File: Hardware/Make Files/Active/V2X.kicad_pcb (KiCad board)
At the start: 2 copper layers, 85 x 56 mm, 216 parts, among them CON1 AVR-PDI-6, IC1 ATXMEGA16A4U-A, J1 DB9, P10 Board Mount 2, P11 Ficudial2, P12 Board Mount 3, P13 Ficudial3, P14 5V0_OUT, P15 Board Mount 4, P16 Ficudial4, P17 CUR_SEN, P19 CUR_SEN, P20 Jumper 1, P21 Jumper 2, P22 CONN_02X04, P23 Jumper 3, P24 Jumper 4, P25 CONN_02X08, P5 NVM_RST, P6 Board Mount 1, P7 Ficudial1, P9 USB_u, Q1 2N7000, Q10 2N3904, Q11 IRF9335, Q13 BSS84, Q14 IRF9335, Q15 2N7000, Q16 2N7000, Q17 2N7000, Q18 2N7000, Q19 2N7000, Q2 BSS84, Q3 BSS84, Q4 BSS84, Q5 3906, Q6 2N3904, Q7 2N7000, Q8 2N3904, Q9 2N3904, SW1 SPST, SW2 SW_PUSH, U1 FT4232H, U10 MCP2551, U11 XRP6124, U12 SLG59M, U15 SLG59M, U16 SLG59M, U17 XRP6124, U18 SLG59M, U19 ADXL345, U2 93C46, U20 USB2242, U21 74LS126, U22 74HC595, U23 74HC595, U5 ESDAxxSC6, U6 ESDAxxSC6, U7 STN1110, U8 LM339, U9 LM317, X1 12MHz, X2 16MHz, X3 24MHz

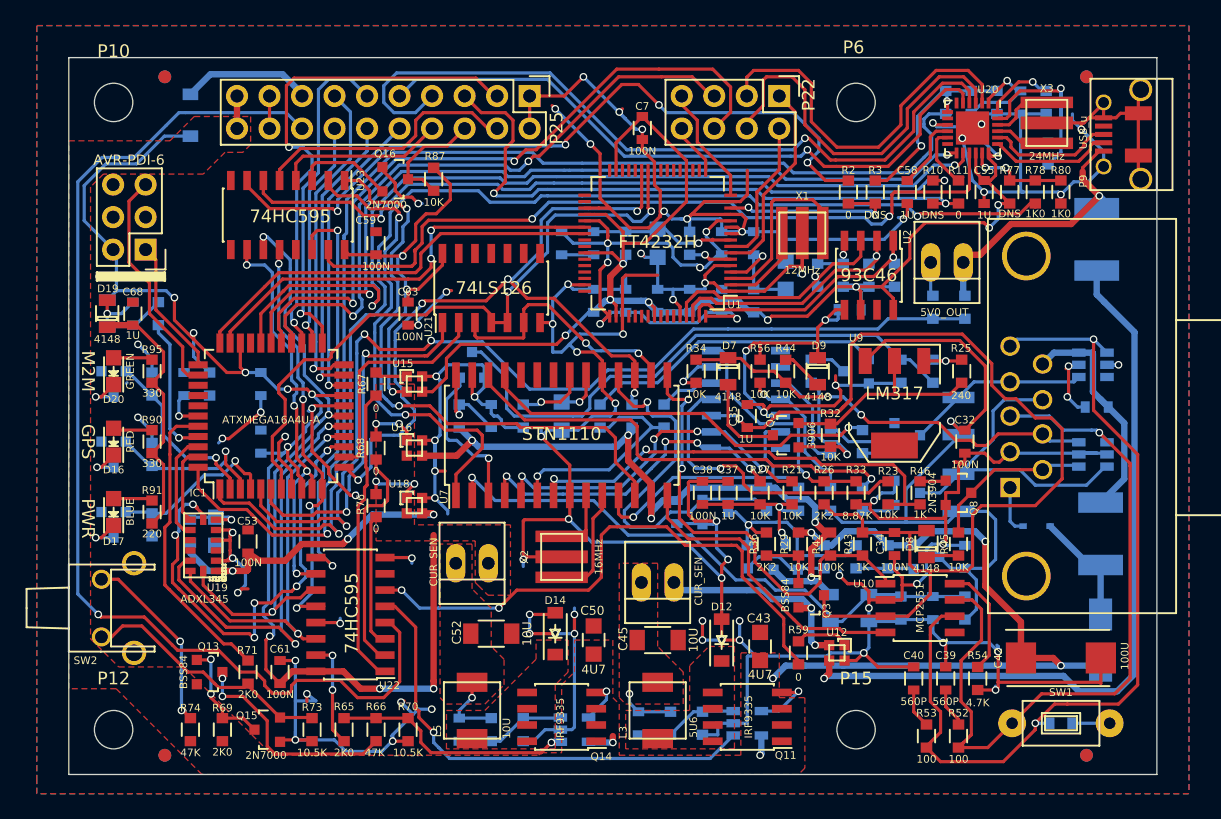
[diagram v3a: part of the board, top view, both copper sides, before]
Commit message: Added USB-A to design
discovered the Rpi cannot be back fed over USB, had to add a power Port
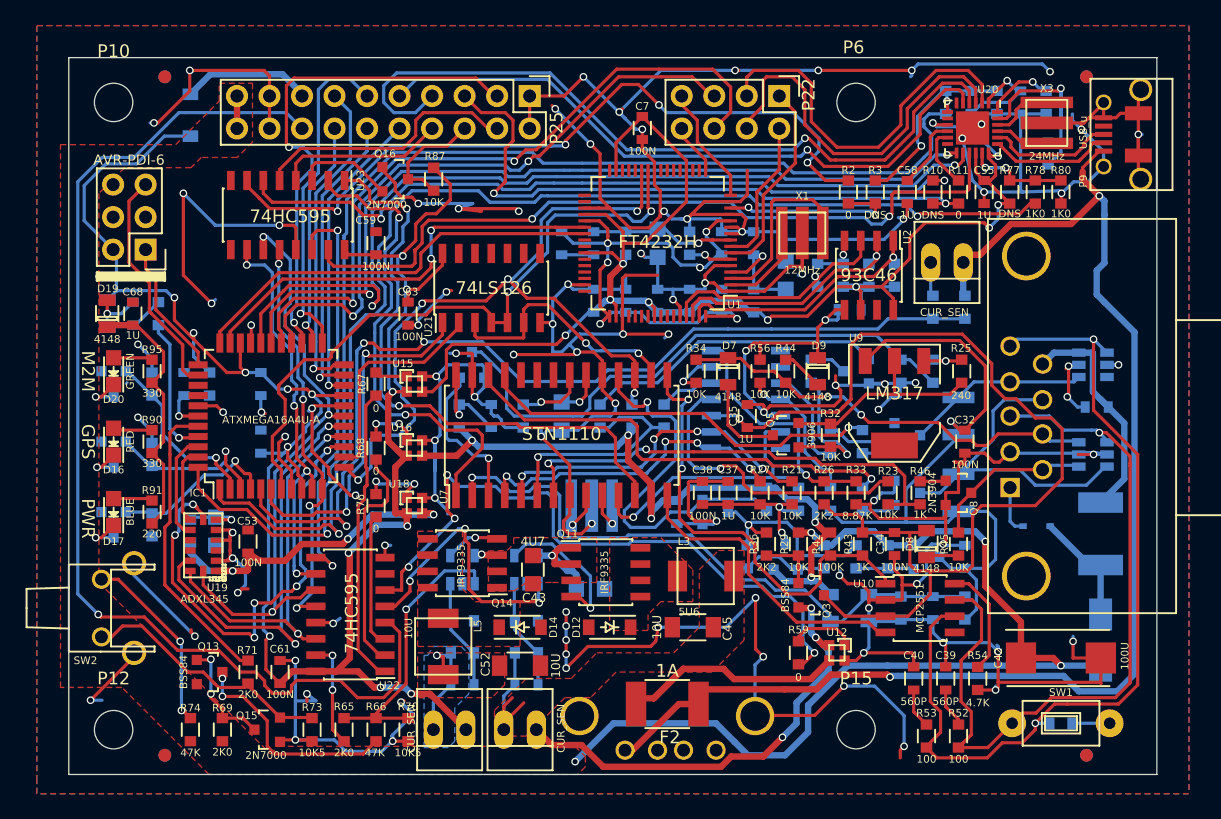
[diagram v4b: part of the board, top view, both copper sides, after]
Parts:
- added P8: USB_A, Connect:USB_A, B.Cu at (78.7, 177.1)
- C50, X2: moved to B.Cu
- F1: value 1.1A -> 1.25A
- F2: moved to F.Cu
- P14: value 5V0_OUT -> CUR_SEN
- R62, R70, R73: value 10.5K -> 10K5
- moved F2 49.4 mm to (82.0, 173.5), turned to 0 degrees
- moved U11 21.0 mm to (71.0, 163.0), turned to 90 degrees
- moved C43 18.7 mm to (71.5, 163.0), turned to 270 degrees
- moved R61 15.9 mm to (71.0, 167.0), turned to 180 degrees
- moved Q11 15.8 mm to (77.2, 163.2), turned to 0 degrees
- moved P17 15.7 mm to (70.5, 175.5)
- moved U17 15.3 mm to (66.0, 163.0), turned to 90 degrees
- moved Q14 14.3 mm to (66.0, 162.5)
- moved P19 13.1 mm to (65.0, 175.5)
- moved R62 12.5 mm to (71.0, 169.5), turned to 180 degrees
- moved L3 11.1 mm to (85.0, 163.5), turned to 0 degrees
- moved R75 9.74 mm to (66.0, 167.0), turned to 0 degrees
- moved C44 9.25 mm to (71.0, 172.0), turned to 0 degrees
- moved D12 8.81 mm to (77.5, 167.5), turned to 180 degrees
- moved R72 6.41 mm to (66.0, 169.5), turned to 0 degrees
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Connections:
- net CAN_RXD_PS renamed CAN_RXD_SEQ
- CON1 pad 3: (no net) -> Net-(CON1-Pad3)
- CON1 pad 4: (no net) -> Net-(CON1-Pad4)
- IC1 pad 36: (no net) -> Net-(IC1-Pad36)
- IC1 pad 37: (no net) -> Net-(IC1-Pad37)
- J1 pad : GND -> (no net)
- P10 pad 1: (no net) -> Net-(P10-Pad1)
- P12 pad 1: (no net) -> Net-(P12-Pad1)
- P14 pad 1: 5V0_B_OUT -> 4V1_B
- P14 pad 2: GND -> Net-(C46-Pad1)
- P15 pad 1: (no net) -> Net-(P15-Pad1)
- P6 pad 1: (no net) -> Net-(P6-Pad1)
- P9 pad 4: (no net) -> Net-(P9-Pad4)
- U1 pad 18: (no net) -> Net-(U1-Pad18)
- U1 pad 19: (no net) -> Net-(U1-Pad19)
- U1 pad 21: (no net) -> Net-(U1-Pad21)
- U1 pad 22: (no net) -> Net-(U1-Pad22)
- U1 pad 23: (no net) -> Net-(U1-Pad23)
- U1 pad 24: (no net) -> Net-(U1-Pad24)
- U1 pad 28: (no net) -> Net-(U1-Pad28)
- U1 pad 29: (no net) -> Net-(U1-Pad29)
- U1 pad 30: (no net) -> Net-(U1-Pad30)
- U1 pad 32: (no net) -> Net-(U1-Pad32)
- U1 pad 33: (no net) -> Net-(U1-Pad33)
- U1 pad 34: (no net) -> Net-(U1-Pad34)
- U1 pad 40: (no net) -> Net-(U1-Pad40)
- U1 pad 41: (no net) -> Net-(U1-Pad41)
- U1 pad 43: (no net) -> Net-(U1-Pad43)
- U1 pad 44: (no net) -> Net-(U1-Pad44)
- U1 pad 45: (no net) -> Net-(U1-Pad45)
- U1 pad 46: (no net) -> Net-(U1-Pad46)
- U1 pad 48: (no net) -> Net-(U1-Pad48)
- U1 pad 52: (no net) -> Net-(U1-Pad52)
- U1 pad 53: (no net) -> Net-(U1-Pad53)
- U1 pad 54: (no net) -> Net-(U1-Pad54)
- U1 pad 55: (no net) -> Net-(U1-Pad55)
- U1 pad 57: (no net) -> Net-(U1-Pad57)
- U1 pad 58: (no net) -> Net-(U1-Pad58)
- U1 pad 59: (no net) -> Net-(U1-Pad59)
- U10 pad 5: (no net) -> Net-(U10-Pad5)
- U20 pad 12: (no net) -> Net-(U20-Pad12)
- U20 pad 6: (no net) -> Net-(U20-Pad6)
- U20 pad 8: (no net) -> Net-(U20-Pad8)
- U22 pad 7: (no net) -> Net-(U22-Pad7)
- U23 pad 9: (no net) -> Net-(U23-Pad9)
- U6 pad 3: (no net) -> Net-(U6-Pad3)
- U7 pad 22: (no net) -> Net-(U7-Pad22)
- U7 pad 23: (no net) -> Net-(U7-Pad23)
- U7 pad 24: (no net) -> Net-(U7-Pad24)
- U8 pad 14: (no net) -> Net-(U8-Pad14)
- U8 pad 8: (no net) -> Net-(U8-Pad8)
- U8 pad 9: (no net) -> Net-(U8-Pad9)
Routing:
- net GND: track 579.0 -> 668.5 mm, vias 81 -> 99
- net 5V0_B_OUT: track 23.3 -> 99.9 mm, vias 1 -> 2
- net 5V0_B: track 60.0 -> 20.3 mm, vias 1 -> 0
- net 12V0_B: track 63.1 -> 92.1 mm
- net 3V3_A: track 138.8 -> 158.4 mm, vias 12 -> 14
- net 5V0_A: track 16.8 -> 35.9 mm, vias 2 -> 3
- net 5V0_EN: track 37.7 -> 21.7 mm, vias 1 -> 3
- net 5V0_B_EN: track 44.6 -> 52.4 mm, vias 2 -> 4
- net Net-(C44-Pad1): track 4.86 -> 11.9 mm, vias 1 -> 0
- net Net-(Q11-Pad1): track 4.88 -> 11.7 mm
- net CAN_CLKN: track 8.83 -> 3.92 mm, vias 0 -> 1
- net 4V1_B: track 0.00 -> 4.40 mm
- net Net-(C51-Pad1): track 5.71 -> 9.69 mm
- net Net-(C46-Pad1): track 0.00 -> 3.76 mm
- net Net-(R65-Pad2): track 18.9 -> 22.0 mm
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- added copper zone on B.Cu, net Net-(C51-Pad1)
- removed copper zone on F.Cu, net 3V3_A

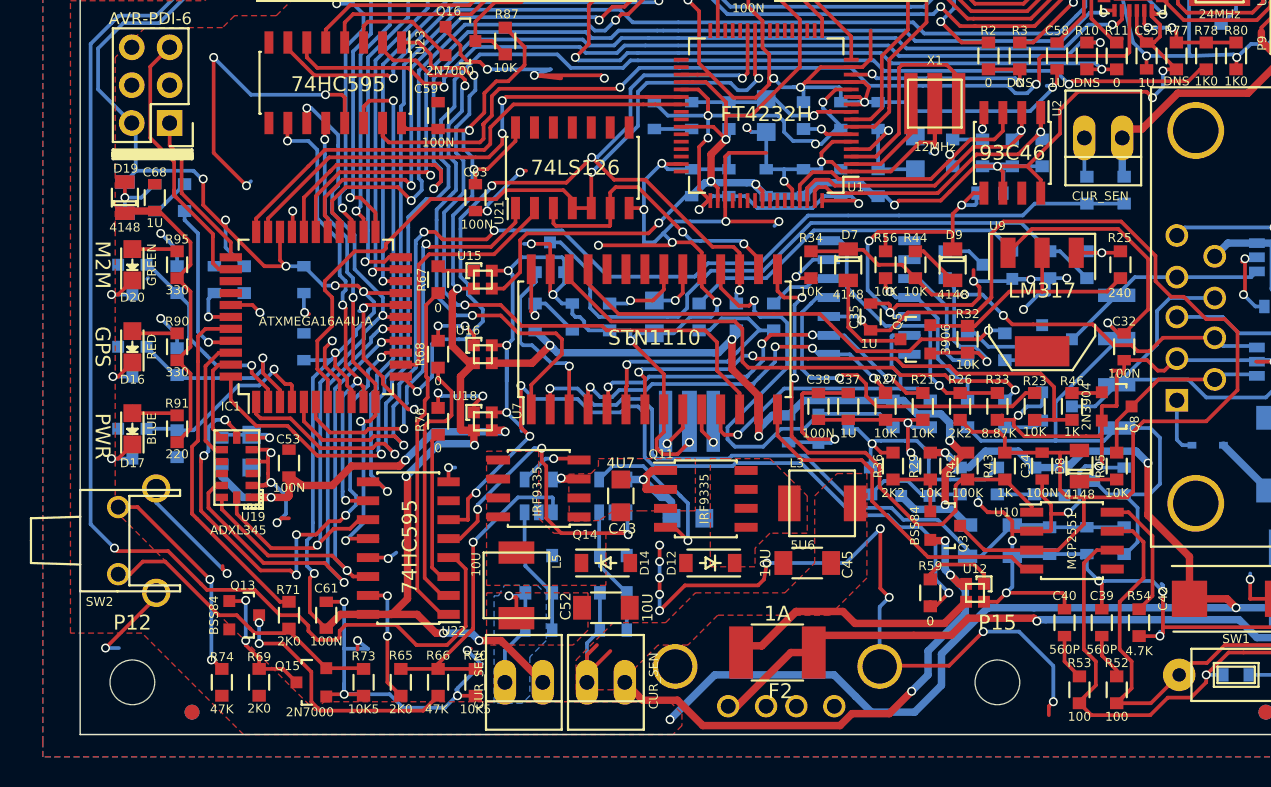
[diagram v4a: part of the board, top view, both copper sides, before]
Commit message: No Rpi Backpower fix
added a USB-A to the board to power the HOST. fixed LED labeling.
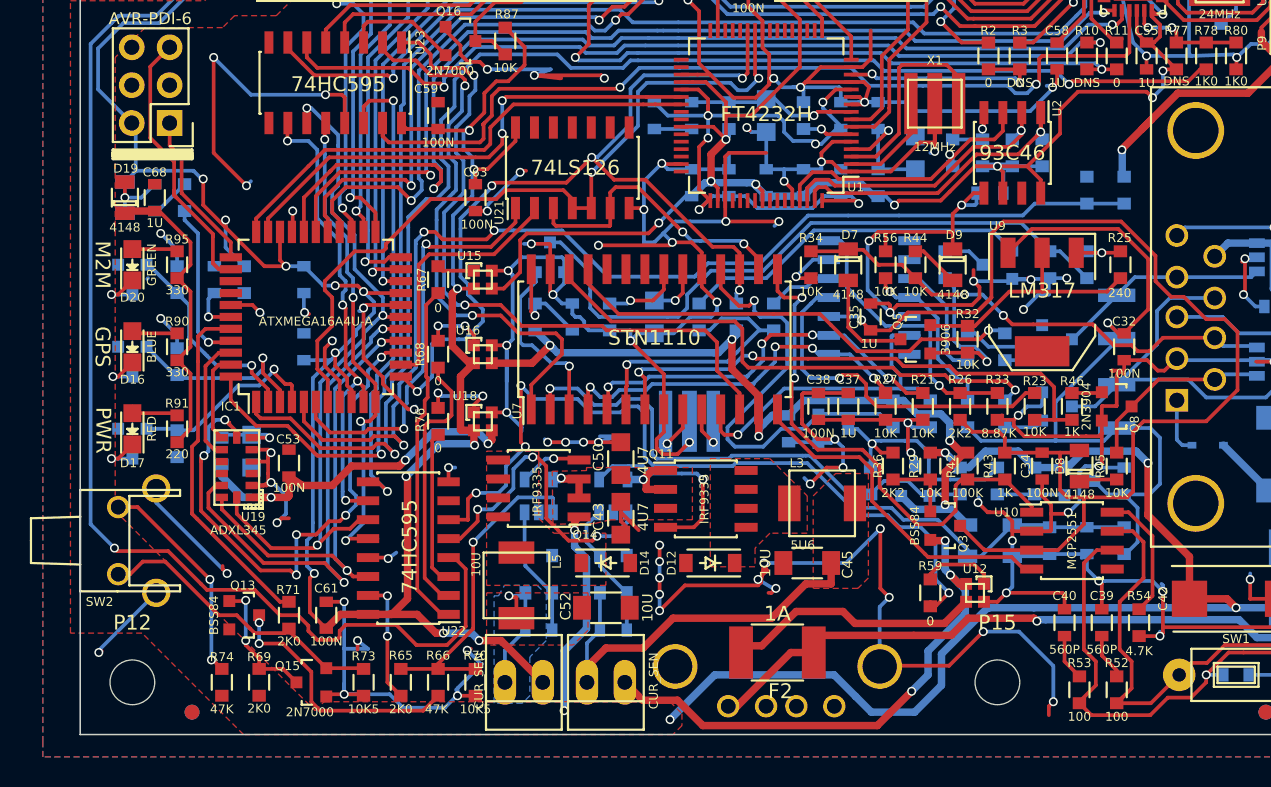
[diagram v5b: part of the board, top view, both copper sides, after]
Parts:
- removed P14: CUR_SEN, Connect:PINHEAD1-2
- C50: moved to F.Cu
- D16: value RED -> BLUE
- D17: value BLUE -> RED
- moved C50 6.02 mm to (71.5, 160.5), turned to 90 degrees
- moved C43 1.50 mm to (71.5, 164.5)
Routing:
- net GND: track 668.5 -> 687.6 mm, vias 99 -> 107
- net Net-(C44-Pad1): track 11.9 -> 28.0 mm
- net 12V0_B: track 92.1 -> 103.5 mm, vias 6 -> 8
- net 5V0_B_OUT: track 99.9 -> 104.5 mm, vias 2 -> 3
- net 4V1_B: track 4.40 -> 0.00 mm
- net Net-(C46-Pad1): track 3.76 -> 0.00 mm
- net 5V0_B: track 20.3 -> 17.1 mm
- net Net-(Q11-Pad1): track 11.7 -> 13.7 mm
- net Net-(C44-Pad2): track 8.67 -> 9.44 mm
- net 3V3_D: track 25.6 -> 24.9 mm
- net 5V0_EN: track 21.7 -> 21.0 mm
- net 5V0_B_EN: track 52.4 -> 53.1 mm
- net CAN_RX: track 23.7 -> 23.1 mm
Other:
- board text added: "JAGUAR LAND ROVER OSTC RVI V2X V1.2 2015"
- board text removed: "JAGUR LAND ROVER OSTC RVI V2X V1.2 2015"

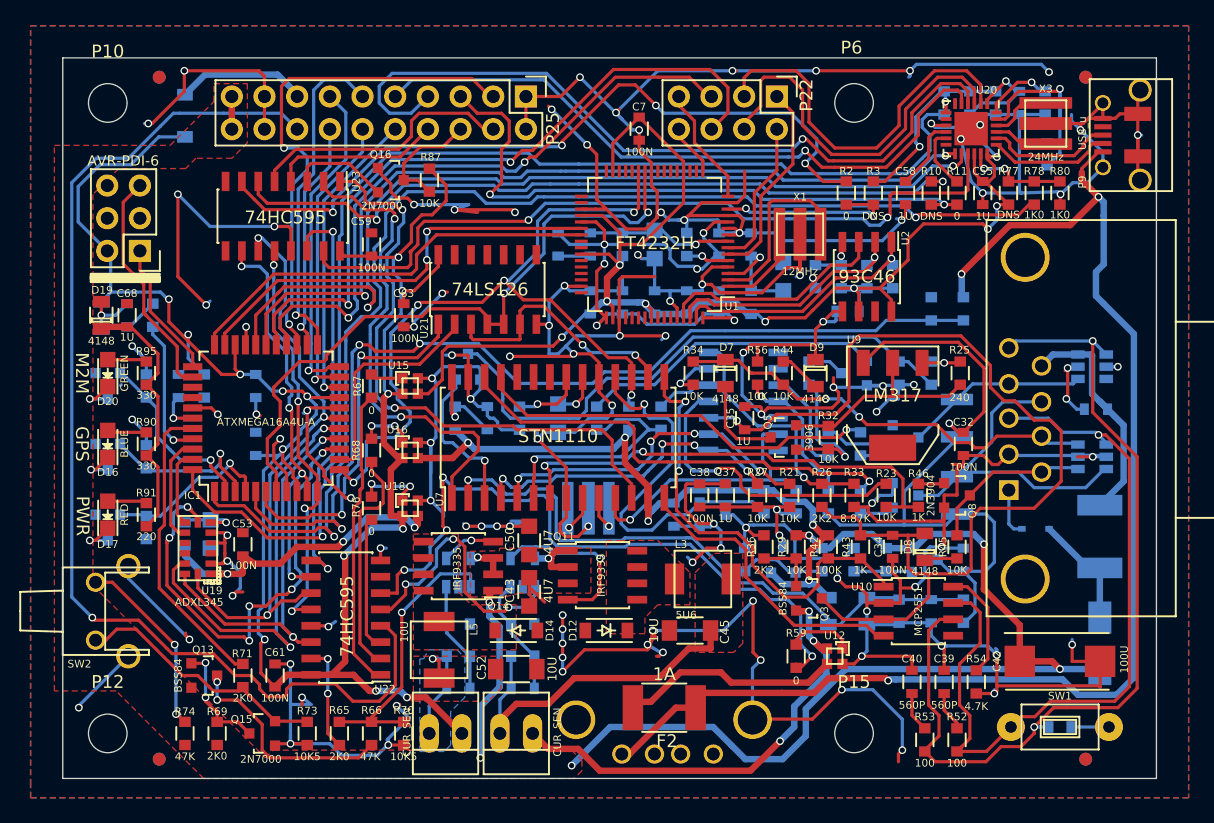
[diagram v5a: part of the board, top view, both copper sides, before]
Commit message: Verification findings and modifications
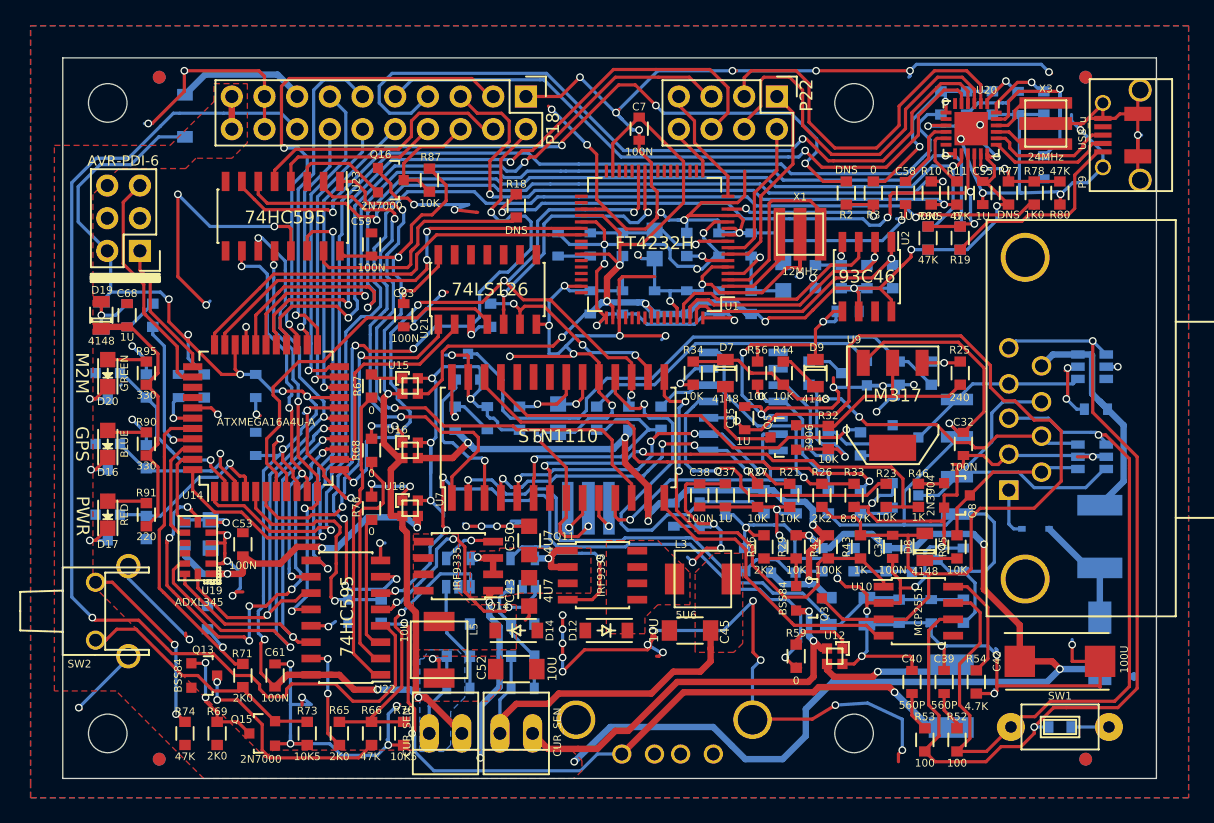
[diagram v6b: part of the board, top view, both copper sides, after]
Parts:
- added C65: 10N, Custom Parts:R_0603_sm, B.Cu at (46.5, 166.5)
- added R18: DNS, Custom Parts:R_0603_sm, F.Cu at (70.5, 134.5)
- added R19: 47K, Custom Parts:R_0603_sm, F.Cu at (105.0, 137.0)
- added R60: 47K, Custom Parts:R_0603_sm, F.Cu at (102.5, 137.0)
- added R63: 1K, Custom Parts:R_0603_sm, B.Cu at (68.5, 143.0)
- added R64: DNS, Custom Parts:R_0603_sm, B.Cu at (102.5, 137.0)
- added R97: DNS, Custom Parts:R_0603_sm, B.Cu at (105.0, 137.0)
- added REF**: Symbol_OSHW-Logo_SilkScreen_BIG, Symbols:Symbol_OSHW-Logo_SilkScreen_BIG, B.Cu at (57.8, 129.8)
- F2: moved to B.Cu
- R2: value 0 -> DNS
- R3: value DNS -> 0
- R80, R83: value 1K0 -> 47K
- moved R88 51.0 mm to (60.0, 166.0), turned to 270 degrees
- moved R89 51.0 mm to (57.5, 166.0), turned to 90 degrees
- moved F2 22.3 mm to (104.3, 172.6), turned to 270 degrees
- moved C56 1.03 mm to (111.5, 131.5), turned to 270 degrees
- moved R81 0.25 mm to (105.5, 126.5)
- moved R82 0.25 mm to (103.5, 126.5)
- moved R83 0.25 mm to (107.5, 126.5)
- moved C57 0.10 mm to (109.5, 126.5)
- moved R79 0.10 mm to (111.5, 126.5)
- turned R2 to 90 degrees
- turned R3 to 270 degrees
- turned R80 to 270 degrees
- renumbered P25 to P18, IC1 to U14
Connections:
- net SEQ-CHGPUMP renamed SEQ_CHGPUMP
- P18 pad 2: GND -> SIM_WAKE
- P9 pad 1: 5V0_B_OUT -> 5V0_HOST
- R2 pad 1: ~FTDI_RESET -> Net-(R2-Pad1)
- R2 pad 2: Net-(R2-Pad2) -> ~FTDI_RESET
- R3 pad 1: Net-(R2-Pad2) -> HUB_PWR_PRT1
- R3 pad 2: HUB_PWR_PRT1 -> Net-(R2-Pad1)
- R80 pad 1: GND -> HUB_SUSP_IND
- R80 pad 2: HUB_SUSP_IND -> GND
- U1 pad 14: Net-(R2-Pad2) -> Net-(R2-Pad1)
- U14 pad 13: CAN_RXD_PS_BUF -> CAN_RXD_SEQ
- U14 pad 6: CAN_RXD_SEQ -> CAN_BUF_SEQ
- U14 pad 7: CAN_RXD_FTDI -> CAN_BUF_FTDI
- U21 pad 1: CAN_RXD_SEQ -> CAN_BUF_SEQ
- U21 pad 2: CAN_RXD_PS_BUF -> CAN_RXD_SEQ
- U21 pad 3: CAN_RXD -> Net-(R63-Pad1)
- U21 pad 4: CAN_RXD_FTDI -> CAN_BUF_FTDI
- U22 pad 7: Net-(U22-Pad7) -> SIM_WAKE
- U23 pad 15: ~HUB_RESET -> HUB_ENABLE
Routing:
- net SIM_WAKE: track 0.00 -> 57.4 mm, vias 0 -> 6
- net HOST_SC: track 75.4 -> 18.5 mm, vias 3 -> 1
- net 5V0_B_OUT: track 104.5 -> 58.7 mm
- net CAN_RXD_FTDI: track 51.7 -> 21.4 mm
- net CAN_BUF_FTDI: track 0.00 -> 29.5 mm
- net CAN_BUF_SEQ: track 0.00 -> 28.0 mm, vias 0 -> 2
- net HUB_ENABLE: track 0.00 -> 19.2 mm
- net CAN_RXD_PS_BUF: track 17.4 -> 0.00 mm
- net 5V0_HOST: track 0.00 -> 17.1 mm
- net Net-(R2-Pad2): track 14.6 -> 0.00 mm, vias 2 -> 0
- net Net-(R2-Pad1): track 0.00 -> 14.6 mm, vias 0 -> 2
- net CAN_RXD_SEQ: track 28.2 -> 17.4 mm, vias 2 -> 0
- net GND: track 687.6 -> 677.1 mm, vias 107 -> 106
- net ~HUB_RESET: track 60.2 -> 50.7 mm, vias 2 -> 4
- net HUB_SDA: track 66.8 -> 73.3 mm
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
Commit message: V2X V1.2 PCB build, with shares
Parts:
- D11: value SD15C -> SMBJ16A; footprint Diodes_SMD:SOD-323 -> Diodes_SMD:SMB_Standard
- moved F1 20.2 mm to (116.0, 140.0)
- moved D11 4.74 mm to (115.5, 160.5), turned to 270 degrees
- moved D10 0.35 mm to (115.5, 168.5)
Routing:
- net Net-(D10-Pad2): track 9.07 -> 29.0 mm
- net GND: track 677.1 -> 678.0 mm
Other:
- board text added: "CAN TERMINATOR"
- board text added: "JAGUAR LAND ROVER OSTC RVI V2X V1.2"
- board text added: "Jesse Banks 2015"
- board text removed: "JAGUAR LAND ROVER OSTC RVI V2X V1.2 2015"
- board text removed: "Jesse Banks"

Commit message: V1.2 Ordered
This is a capture of the project folder at the time f ordering the V1.2
kit.
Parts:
- moved C50 9.62 mm to (76.0, 169.0), turned to 270 degrees
- moved C6 6.35 mm to (102.0, 140.0), turned to 90 degrees
- moved R64 3.35 mm to (104.0, 140.0)
- moved R97 3.16 mm to (106.0, 140.0)
- moved D12 2.05 mm to (79.0, 168.9), turned to 270 degrees
- moved R24 1.80 mm to (102.7, 145.7), turned to 90 degrees
- moved R19 1.00 mm to (105.0, 138.0)
- moved R60 1.00 mm to (102.5, 138.0)
- moved C43 0.40 mm to (71.5, 164.1)
- turned C37 to 270 degrees
- turned C38 to 270 degrees
- turned C69 to 90 degrees
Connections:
- J1 pad : (no net) -> GND
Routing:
- net GND: track 678.0 -> 696.1 mm, vias 106 -> 111
- net Net-(Q11-Pad1): track 13.7 -> 9.57 mm
- net Net-(C51-Pad1): track 9.69 -> 5.62 mm
- net HUB_SDA: track 73.3 -> 76.6 mm
- net 3V3_B: track 129.5 -> 132.4 mm, vias 11 -> 10
- net HUB_SCL: track 77.1 -> 79.2 mm
- net CAN_BUF_FTDI: track 29.5 -> 31.2 mm
- net 12V0_B: track 103.3 -> 104.9 mm
- net 12V0_A: track 18.8 -> 20.3 mm
- net 3V3_A: track 156.6 -> 157.9 mm
- net ~VPW_RX: track 25.1 -> 26.0 mm
- net SIM_WAKE: track 57.4 -> 56.5 mm
- net Net-(R65-Pad2): track 22.5 -> 21.6 mm
- net K-LINE: track 22.5 -> 23.3 mm
- net Net-(C69-Pad2): track 2.75 -> 2.00 mm
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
